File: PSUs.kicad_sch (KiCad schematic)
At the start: 57 parts, among them J6 Barrel_Jack, J7 AMP171826-4, Q1 DMP3013SFV-7, U3 AP64501SP-13, U4 AP64501SP-13, U8 AP62300WU-7

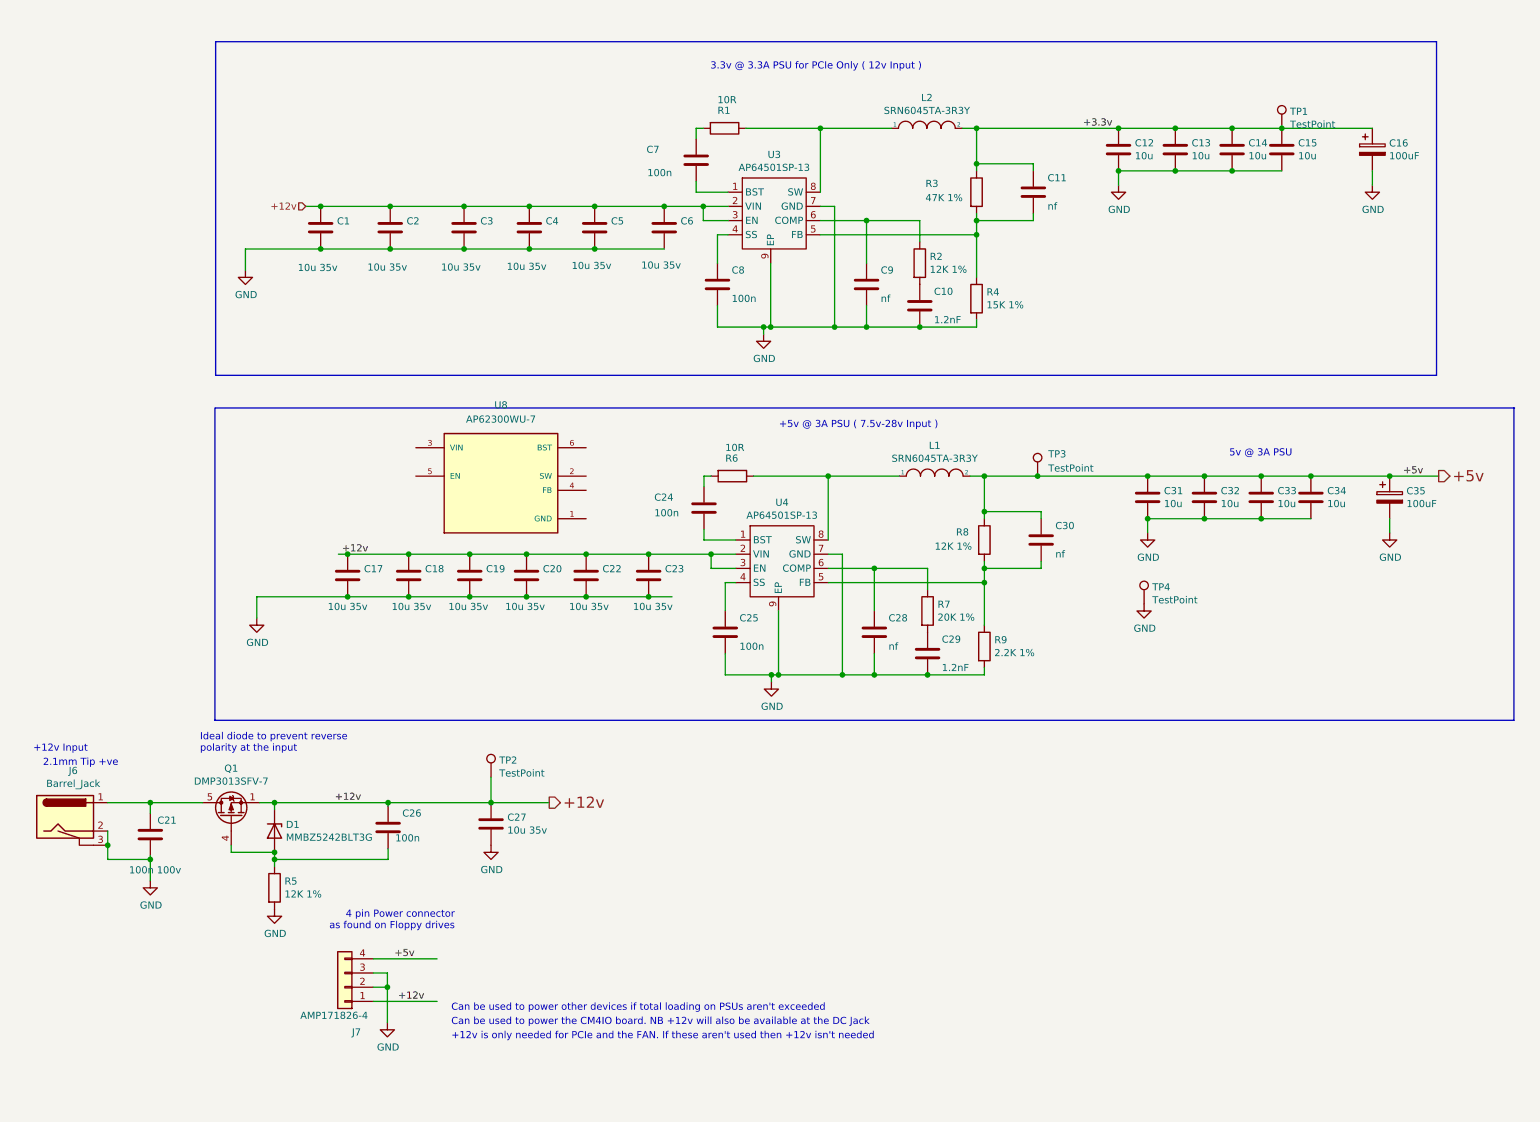
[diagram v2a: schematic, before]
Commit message: USB-c toegeveogd moet alleen nog omvormen
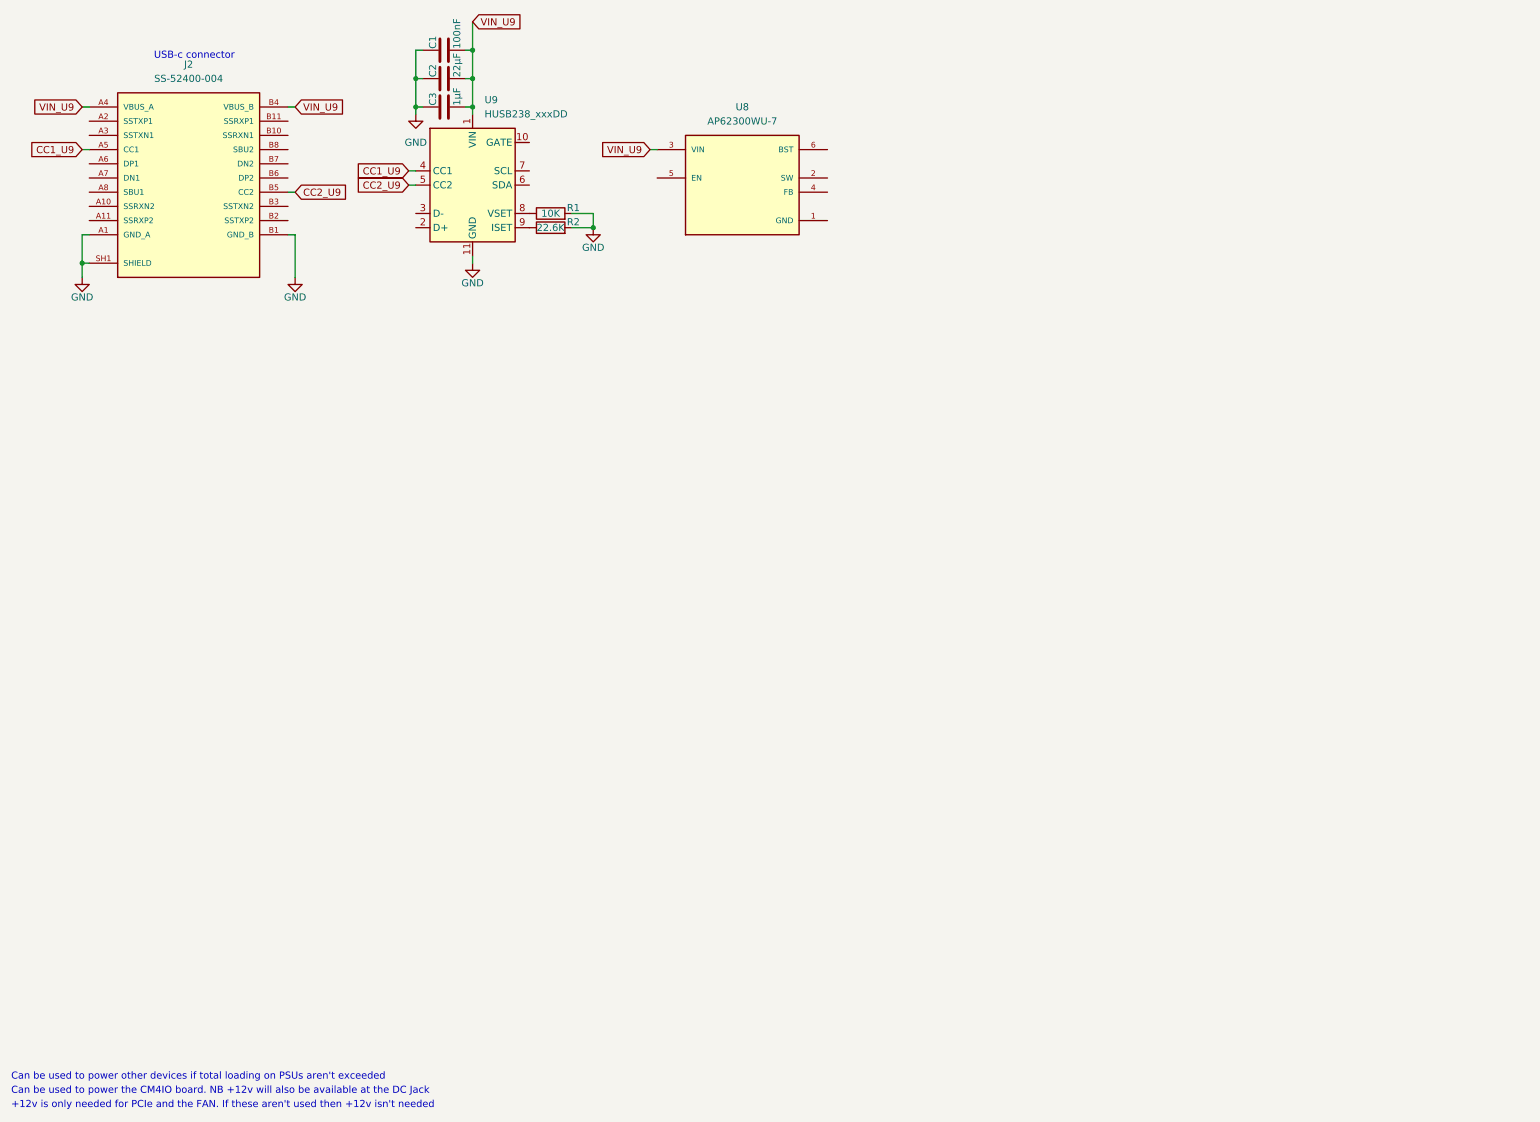
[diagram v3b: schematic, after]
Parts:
- removed C10, C29: 1.2nF, Capacitor_SMD:C_0402_1005Metric, symbol Device:C
- removed C11, C28, C30, C9: nf, Capacitor_SMD:C_0402_1005Metric, symbol Device:C
- removed C12, C13, C14, C15, C31, C32, C33, C34: 10u, Capacitor_SMD:C_0805_2012Metric, symbol Device:C
- removed C16, C35: 100uF, Capacitor_Tantalum_SMD:CP_EIA-7343-31_Kemet-D, symbol Device:CP
- removed C17, C18, C19, C20, C22, C23, C27, C4, C5, C6: 10u 35v, Capacitor_SMD:C_0805_2012Metric, symbol Device:C
- removed C21: 100n 100v, Capacitor_SMD:C_0402_1005Metric, symbol Device:C
- removed C24, C25, C26, C7, C8: 100n, Capacitor_SMD:C_0402_1005Metric, symbol Device:C
- removed D1: MMBZ5242BLT3G, Diode_SMD:D_SOT-23_ANK, symbol Diode:BZX84Cxx
- removed J6: Barrel_Jack, CM4IO:BarrelJack_Horizontal, symbol CM4IO:Barrel_Jack
- removed J7: AMP171826-4, 171826-4:TE_171826-4, symbol Connector_Generic:Conn_01x04
- removed L1, L2: SRN6045TA-3R3Y, Inductor_SMD:L_Bourns_SRN6045TA, symbol pspice:INDUCTOR
- removed Q1: DMP3013SFV-7, Package_SON:Diodes_PowerDI3333-8, symbol Transistor_FET:DMP3013SFV
- removed R3: 47K 1%, Resistor_SMD:R_0402_1005Metric, symbol Device:R
- removed R4: 15K 1%, Resistor_SMD:R_0402_1005Metric, symbol Device:R
- removed R5, R8: 12K 1%, Resistor_SMD:R_0402_1005Metric, symbol Device:R
- removed R6: 10R, Resistor_SMD:R_0402_1005Metric, symbol Device:R
- removed R7: 20K 1%, Resistor_SMD:R_0402_1005Metric, symbol Device:R
- removed R9: 2.2K 1%, Resistor_SMD:R_0402_1005Metric, symbol Device:R
- removed TP1, TP2, TP3, TP4: TestPoint, TestPoint:TestPoint_Pad_2.0x2.0mm, symbol Connector:TestPoint
- removed U3: AP64501SP-13, CM4IO:SOIC-8-1EP_3.9x4.9mm_P1.27mm_EP2.95x4.9mm_Mask2.71x3.4mm_ThermalVias, symbol CM4IO:AP64351
- removed U4: AP64501SP-13, Package_SO:SOIC-8-1EP_3.9x4.9mm_P1.27mm_EP2.95x4.9mm_Mask2.71x3.4mm_ThermalVias, symbol CM4IO:AP64351
- added J2: SS-52400-004, SS-52400-004:STEWART_SS-52400-004 (USB-C), symbol SS-52400-004:SS-52400-004
- added U9: HUSB238_xxxDD, Package_DFN_QFN:WDFN-10-1EP_3x3mm_P0.5mm_EP1.8x2.5mm, symbol Interface_USB:HUSB238_xxxDD
- C1: value 10u 35v -> 100nF; footprint Capacitor_SMD:C_0805_2012Metric -> (none); Field4 Digikey -> (none); Field5 490-10505-1-ND -> (none); Field6 GRM21BC8YA106KE11L -> (none); Field7 Murata -> (none); Part Description 10uF 10% or 20% 35V Ceramic Capacitor X6S 0805 (2012 Metric) -> (none)
- C2: value 10u 35v -> 22µF; footprint Capacitor_SMD:C_0805_2012Metric -> (none); Field4 Digikey -> (none); Field5 490-10505-1-ND -> (none); Field6 GRM21BC8YA106KE11L -> (none); Field7 Murata -> (none); Part Description 10uF 10% or 20% 35V Ceramic Capacitor X6S 0805 (2012 Metric) -> (none)
- C3: value 10u 35v -> 1µF; footprint Capacitor_SMD:C_0805_2012Metric -> (none); Field4 Digikey -> (none); Field5 490-10505-1-ND -> (none); Field6 GRM21BC8YA106KE11L -> (none); Field7 Murata -> (none); Part Description 10uF 10% or 20% 35V Ceramic Capacitor X6S 0805 (2012 Metric) -> (none)
- R1: value 10R -> 10K; footprint Resistor_SMD:R_0402_1005Metric -> (none); Field4 Farnell -> (none); Field5 9238999 -> (none); Field6 RC0402FR-0710RL -> (none); Field7 Yageo -> (none); Field8 URES00256 -> (none); Part Description Resistor 10R M1005 1% 63mW -> (none)
- R2: value 12K 1% -> 22.6K; footprint Resistor_SMD:R_0402_1005Metric -> (none); Field4 Farnell -> (none); Field5 9239367 -> (none); Field6 MCR01MZPF1202 -> (none); Field7 Rohm -> (none); Part Description Resistor 12K M1005 1% 63mW -> (none)
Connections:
- net +12v is gone; now on net GND: C1.1, C2.1, C3.1
- net GND: now also R1.2, R2.2, J2.A1 (GND_A), J2.A12 (GND_A), J2.B1 (GND_B), J2.B12 (GND_B), J2.SH1 (SHIELD), J2.SH2 (SHIELD), J2.SH3 (SHIELD), J2.SH4 (SHIELD), U9.11 (GND); no longer C1.2, C2.2, C3.2
- net at R1.1: now also U9.8 (VSET)
- net at R2.1: now also U9.9 (ISET)
- net VBUS_A: now reaches U8.3 (VIN)
- net VBUS_A: now also C1.2, C2.2, C3.2, J2.A4 (VBUS_A), J2.A9 (VBUS_A), J2.B4 (VBUS_B), J2.B9 (VBUS_B), U9.1 (VIN)
- new net CC1_U9: J2.A5 (CC1), U9.4 (CC1)
- new net CC2_U9: J2.B5 (CC2), U9.5 (CC2)
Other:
- note added: "USB-c connector"
- note removed: "+12v Input"
- note removed: "+5v @ 3A PSU ( 7.5v-28v Input )"
- note removed: "2.1mm Tip +ve"
- note removed: "3.3v @ 3.3A PSU for PCIe Only ( 12v Input )"
- note removed: "4 pin Power connector as found on Floppy drives"
- note removed: "5v @ 3A PSU"
- note removed: "Ideal diode to prevent reverse polarity at the input"
- moved on the sheet: U8

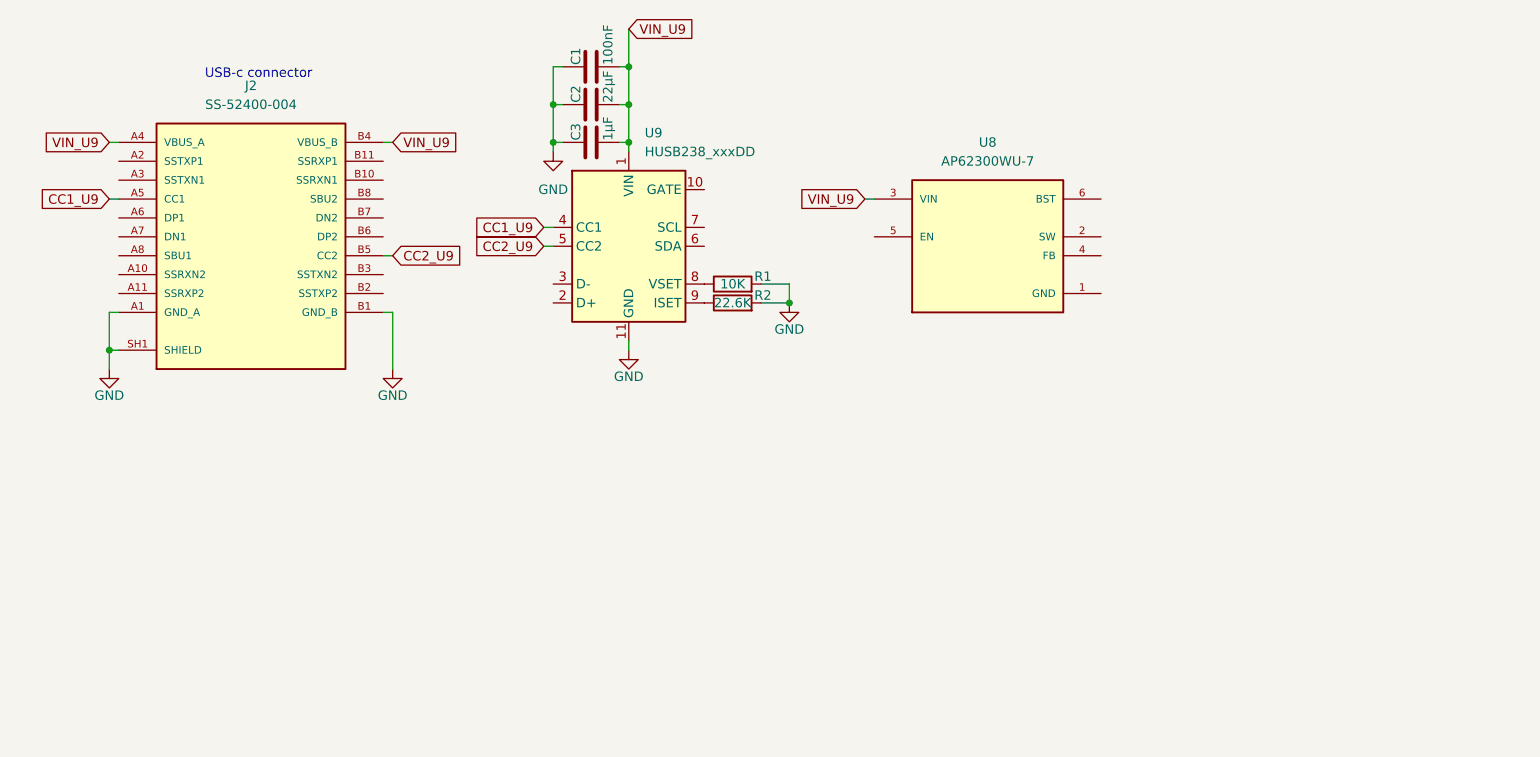
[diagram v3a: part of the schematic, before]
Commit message: USB-C afgemaakt
Ik heb hem apart gepusht. ik ga nu bezig zijn met de HDMI
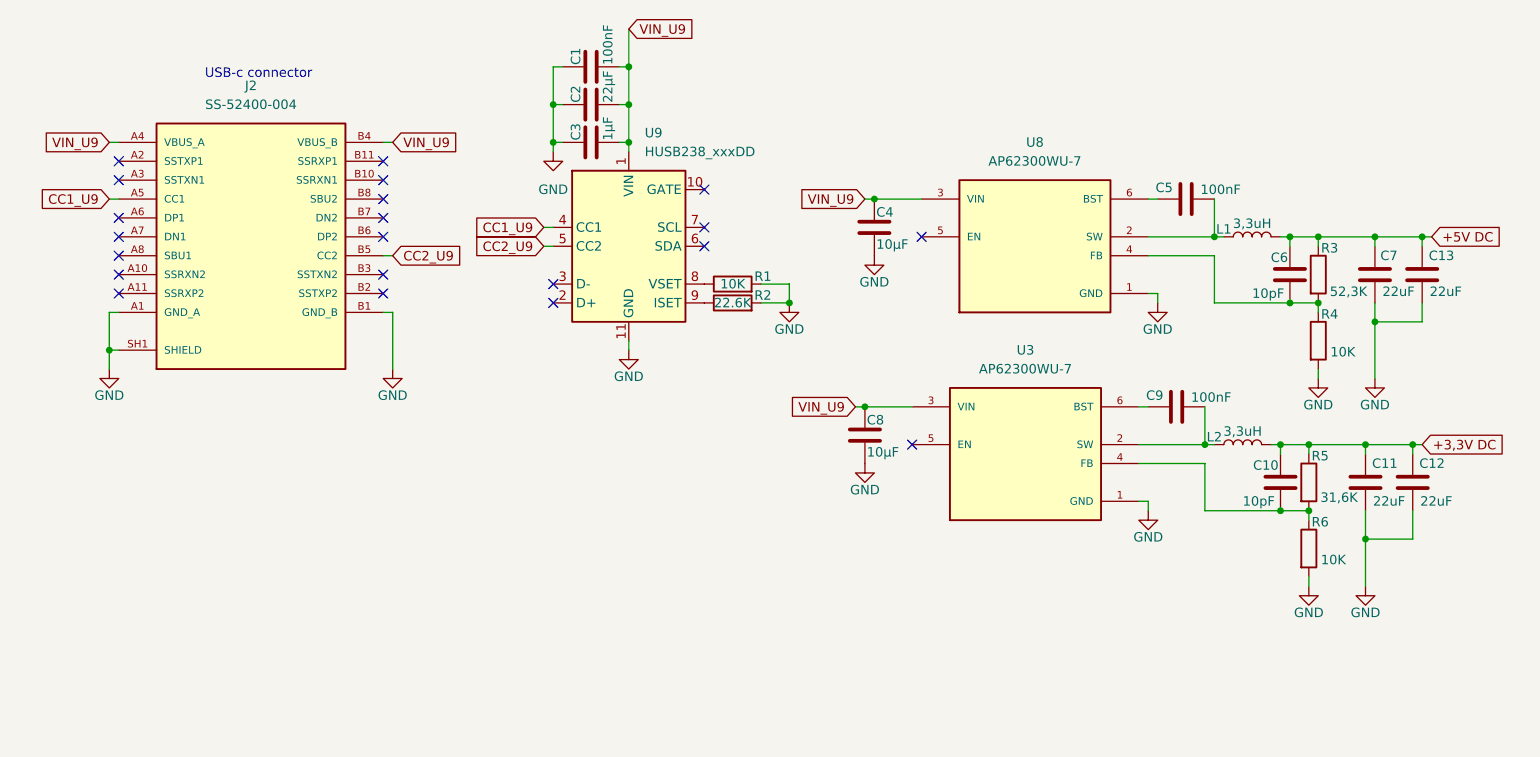
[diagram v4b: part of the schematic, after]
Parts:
- added C10, C6: 10pF, symbol Device:C
- added C11, C12, C13, C7: 22uF, symbol Device:C
- added C4, C8: 10µF, symbol Device:C
- added C5, C9: 100nF, symbol Device:C
- added L1, L2: 3,3uH, symbol Device:L
- added R3: 52,3K, symbol Device:R
- added R4, R6: 10K, symbol Device:R
- added R5: 31,6K, symbol Device:R
- added U3: AP62300WU-7, AP62300WU-7:SOT95P280X100-6N, symbol AP62300WU-7:AP62300WU-7
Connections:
- net GND: now also U8.1 (GND), C11.1, C12.1, C13.1, C4.2, C7.1, C8.2, R4.2, R6.2, U3.1 (GND)
- net VBUS_A: now also C4.1, C8.1, U3.3 (VIN)
- net at U8.2 (SW): now also C5.2, L1.1
- net at U8.4 (FB): now also C6.1, R3.2, R4.1
- net at U8.6 (BST): now also C5.1
- new net: C9.1, U3.6 (BST)
- new net: C9.2, L2.1, U3.2 (SW)
- new net: C10.1, R5.2, R6.1, U3.4 (FB)
- new net +3,3V DC: C10.2, C11.2, C12.2, L2.2, R5.1
- new net +5V DC: C13.2, C6.2, C7.2, L1.2, R3.1
- no-connect marks 0 -> 21
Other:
- moved on the sheet: U8

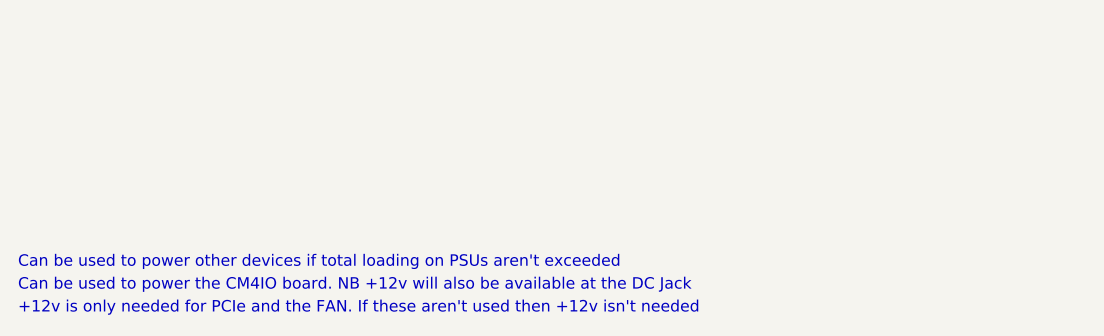
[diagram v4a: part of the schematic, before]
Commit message: Heb mijn documentatie geleverd voor de USB-c en heb een BOM toegevoegd
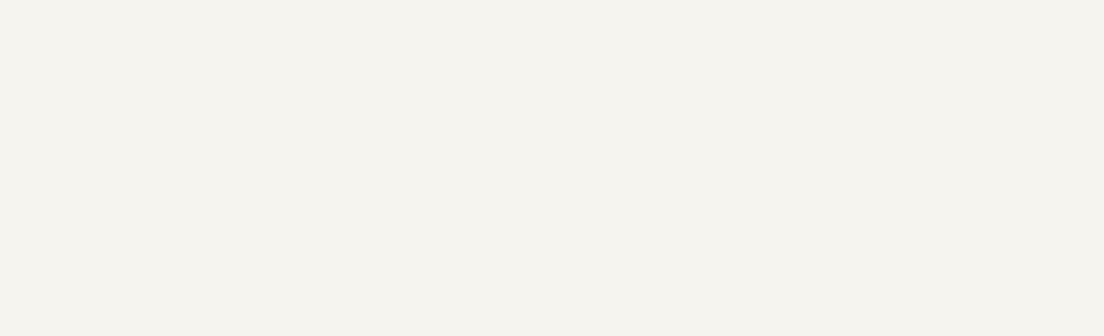
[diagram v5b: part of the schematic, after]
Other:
- note removed: "+12v is only needed for PCIe and the FAN. If these aren't used then +12v isn't needed"
- note removed: "Can be used to power other devices if total loading on PSUs aren't exceeded"
- note removed: "Can be used to power the CM4IO board. NB +12v will also be available at the DC Jack"
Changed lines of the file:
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@@
 	(generator_version "9.0")
 	(paper "A4")
-	(text "Can be used to power the CM4IO board. NB +12v will also be available at the DC Jack"
-		(exclude_from_sim no)
-		(at 10.16 205.994 0)
-		(effects
-			(font
-				(size 1.27 1.27)
-			)
-			(justify left bottom)
-		)
-	)
-	(text "Can be used to power other devices if total loading on PSUs aren't exceeded"
-		(exclude_from_sim no)
-		(at 10.16 203.454 0)
-		(effects
-			(font
-				(size 1.27 1.27)
-			)
-			(justify left bottom)
-		)
-	)
 	(text "USB-c connector\n"
 		(exclude_from_sim no)
@@
 		)
 	)
-	(text "+12v is only needed for PCIe and the FAN. If these aren't used then +12v isn't needed"
-		(exclude_from_sim no)
-		(at 10.16 208.534 0)
-		(effects
-			(font
-				(size 1.27 1.27)
-			)
-			(justify left bottom)
-		)
-	)
